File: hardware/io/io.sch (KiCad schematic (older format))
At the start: 19 parts, among them P1 CONN_IO, P2 CONN_01X04, P3 CONN_USB, P4 CONN_01X08, U1 74LS125, U10 74LS173, U2 74LS32, U3 74LS173, U4 74LS00, U5 74LS173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

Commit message: IO board
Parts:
- removed P2: CONN_01X04, symbol CONN_01X04
- added C10, C11, C12, C3, C4, C5, C6, C7, C8, C9: C, Capacitors_ThroughHole:C_Disc_D3_P2.5, symbol C
- added P2: CONN_01X02, Pin_Headers:Pin_Header_Straight_1x02, symbol CONN_01X02
- added unit 1 of U4
- C1: footprint (none) -> Capacitors_ThroughHole:C_Disc_D6_P5; symbol CP1 -> C
- C2: footprint (none) -> Capacitors_ThroughHole:C_Disc_D3_P2.5; symbol CP1 -> C
- DS1: footprint WC1602A -> Display:RC1602A
- P1, P3: footprint (none) -> Socket_Strips:Socket_Strip_Straight_2x10
- P4: footprint (none) -> Pin_Headers:Pin_Header_Straight_1x08
- R1: footprint (none) -> Resistors_ThroughHole:Resistor_Horizontal_RM10mm
- RV1: footprint (none) -> Potentiometers:Potentiometer_Trimmer-Suntan-TSR-3386P
- U1, U2, U4, U7, U8: footprint (none) -> Housings_DIP:DIP-14_W7.62mm
- U10, U3, U5, U6: footprint (none) -> Housings_DIP:DIP-16_W7.62mm
- U9: footprint (none) -> Housings_DIP:DIP-18_W7.62mm
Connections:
- net GND: now also C10.1, C11.1, C12.1, C3.1, C4.1, C5.1, C6.1, C7.1, C8.1, C9.1, P2.2 (P2), U4.7 (GND)
- net VCC: now also C10.2, C11.2, C12.2, C3.2, C4.2, C5.2, C6.2, C7.2, C8.2, C9.2, P2.1 (P1), U4.14 (VCC)
- net ~USB_RD: now also U4.6; no longer U3.5 (Q2), U4.1, U4.2
- net ~USB_WR: now also U4.3; no longer U3.6 (Q3)
- net at U5.1 (Oe1), U5.2 (Oe2), U6.1 (Oe1)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: now also U3.5 (Q2), U4.4, U4.5; no longer U4.3
- new net: U3.6 (Q3), U4.1, U4.2
- no-connect marks 16 -> 15

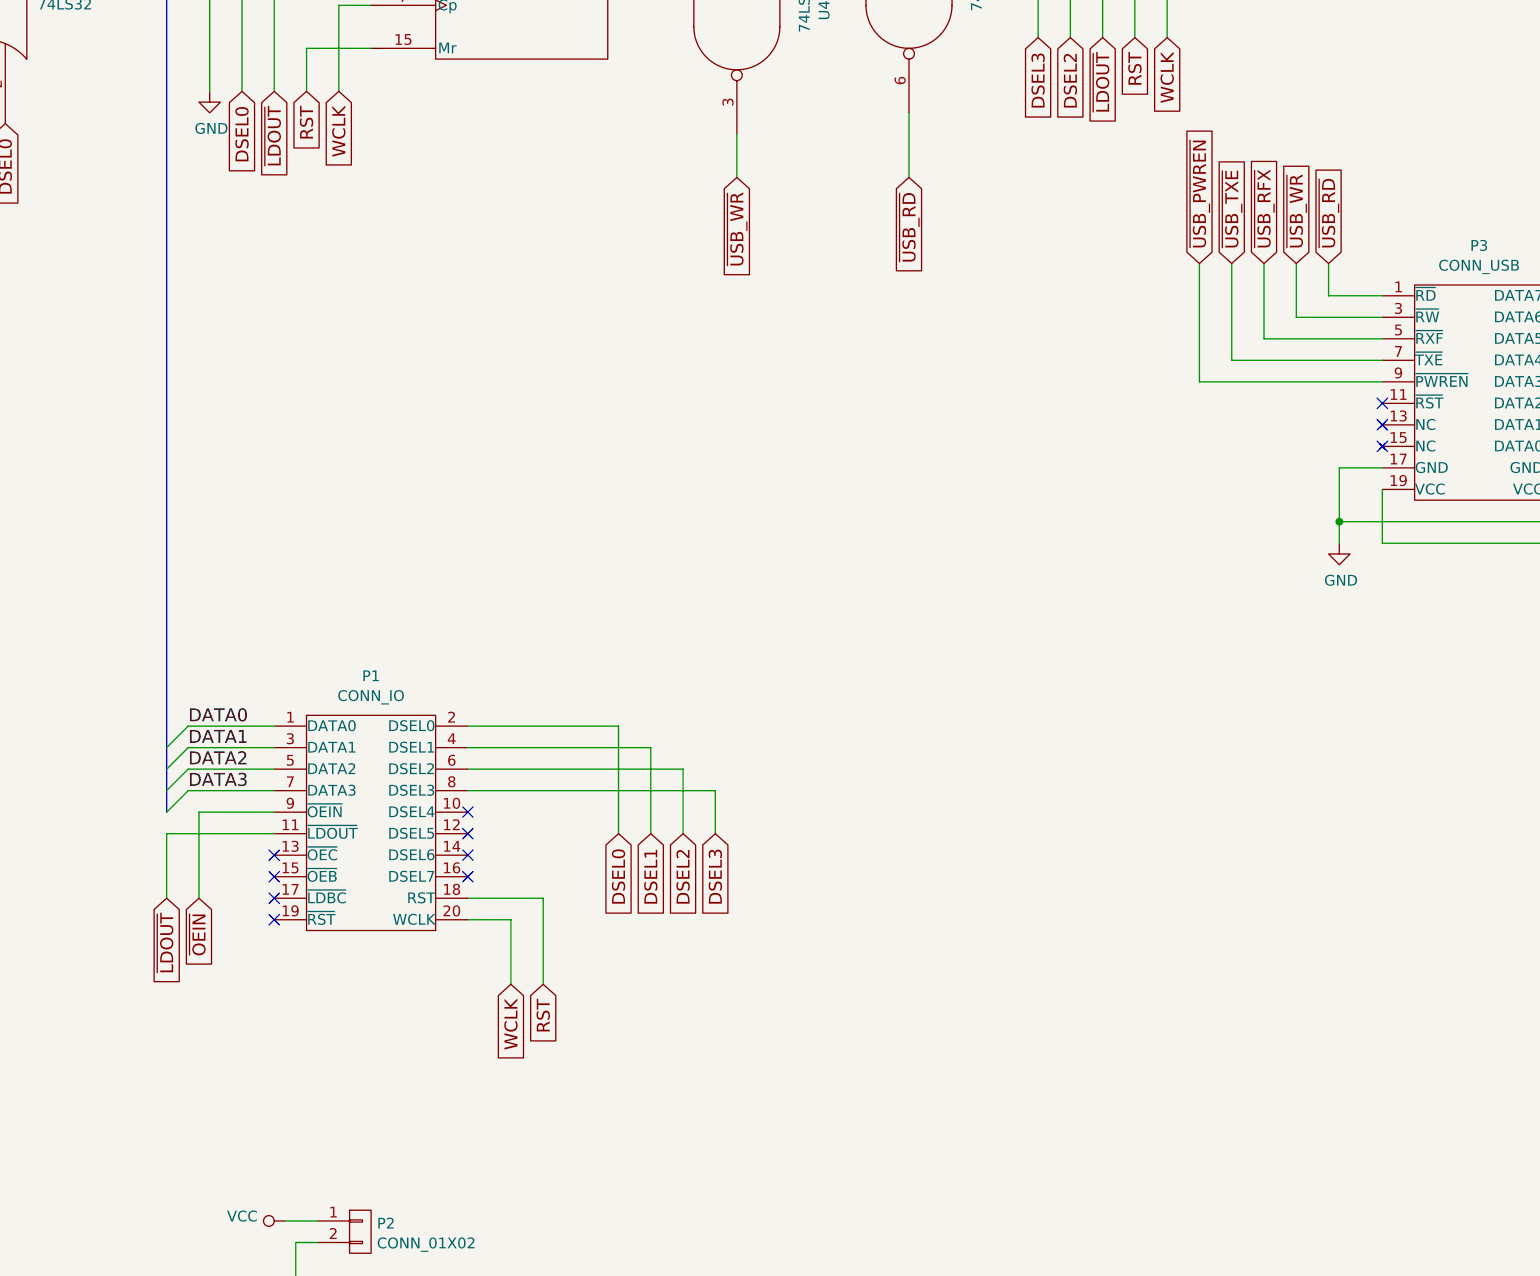
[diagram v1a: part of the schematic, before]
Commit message: Supply ~RST to USB interface
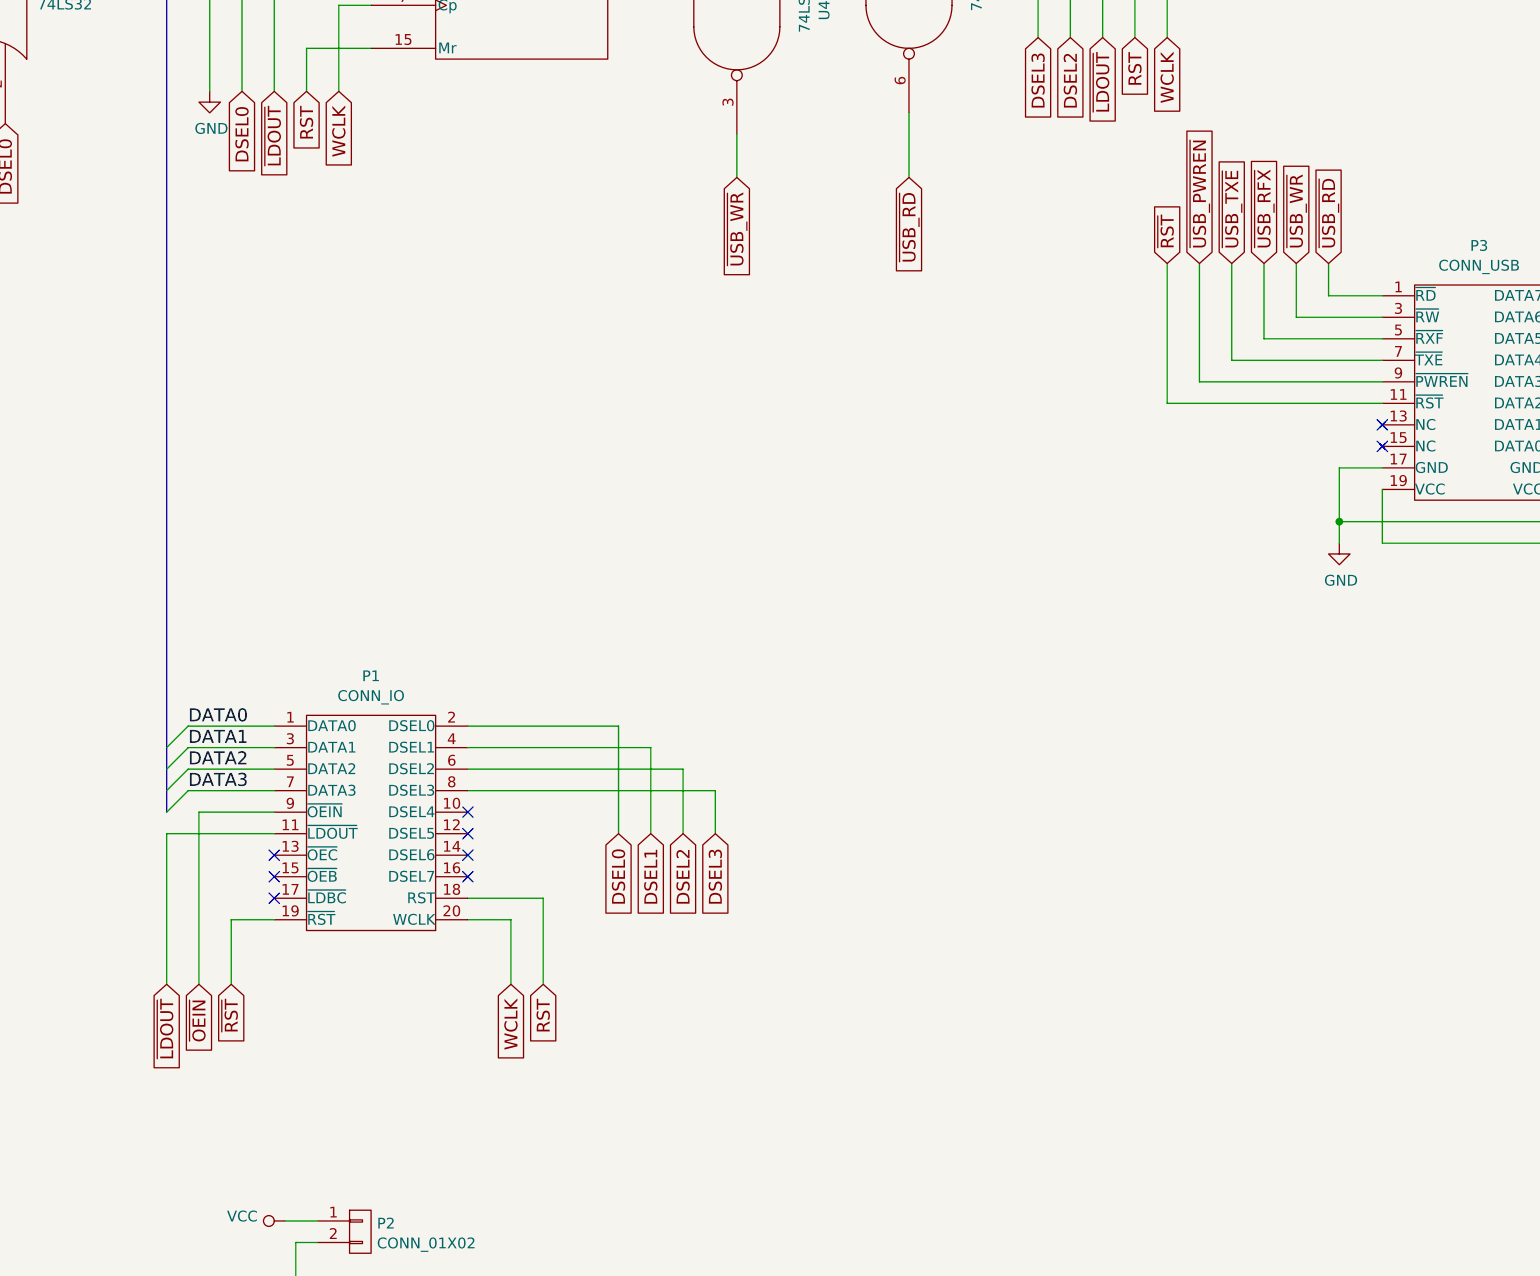
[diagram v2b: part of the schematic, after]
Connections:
- net ~RST: now reaches P1.19 (~RST)
- net ~RST: now also P3.11 (~RST)
- no-connect marks 15 -> 13
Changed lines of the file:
@@
 Text GLabel 4850 8750 3    60   Input ~ 0
 WCLK
-Text GLabel 3400 8350 3    60   Input ~ 0
+Text GLabel 3400 8750 3    60   Input ~ 0
 ~OEIN
-Text GLabel 3250 8350 3    60   Input ~ 0
+Text GLabel 3250 8750 3    60   Input ~ 0
 ~LDOUT
 Text Label 3350 7550 0    60   ~ 0
@@
 NoConn ~ 3750 8250
 NoConn ~ 3750 8350
-NoConn ~ 3750 8450
 $Comp
 L 74LS125 U1
@@
 	1    0    0    -1
 $EndComp
-NoConn ~ 8900 6050
 $Comp
 L GND #PWR015
@@
 	15950 7200 16200 7200
 Wire Wire Line
-	3400 8350 3400 7950
+	3400 7950 3400 8750
 Wire Wire Line
 	3400 7950 3750 7950
 Wire Wire Line
-	3250 8350 3250 8050
+	3250 8050 3250 8750
 Wire Wire Line
 	3250 8050 3750 8050
@@
 Wire Wire Line
 	3850 9950 3850 10150
+Text GLabel 3550 8750 3    60   Input ~ 0
+~RST
+Wire Wire Line
+	3550 8750 3550 8450
+Wire Wire Line
+	3550 8450 3750 8450
+Text GLabel 7900 5400 1    60   Input ~ 0
+~RST
+Wire Wire Line
+	7900 5400 7900 6050
+Wire Wire Line
+	7900 6050 8900 6050
 $EndSCHEMATC
